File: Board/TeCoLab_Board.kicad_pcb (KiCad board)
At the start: 2 copper layers, 95.1 x 93.8 mm, 61 parts, among them J1 Jack, J2 Supply_Terminal, J3 DC Cooler, Q1 BC337, Q2 TIP122, Q3 TIP122, U1 DS18B20, U2 PC817, U3 DS18B20, U4 DS18B20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

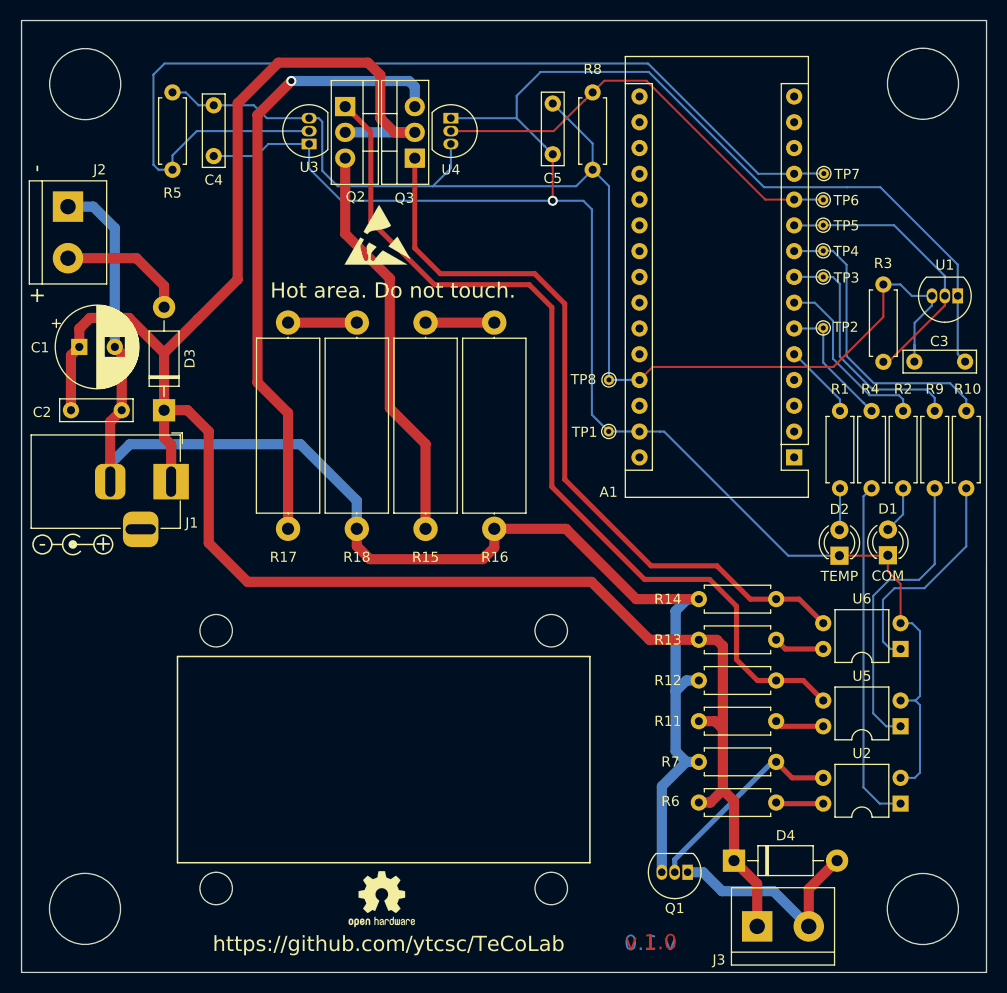
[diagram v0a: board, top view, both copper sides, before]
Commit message: Hardware: Update files to comply with KiCad version 8.0.
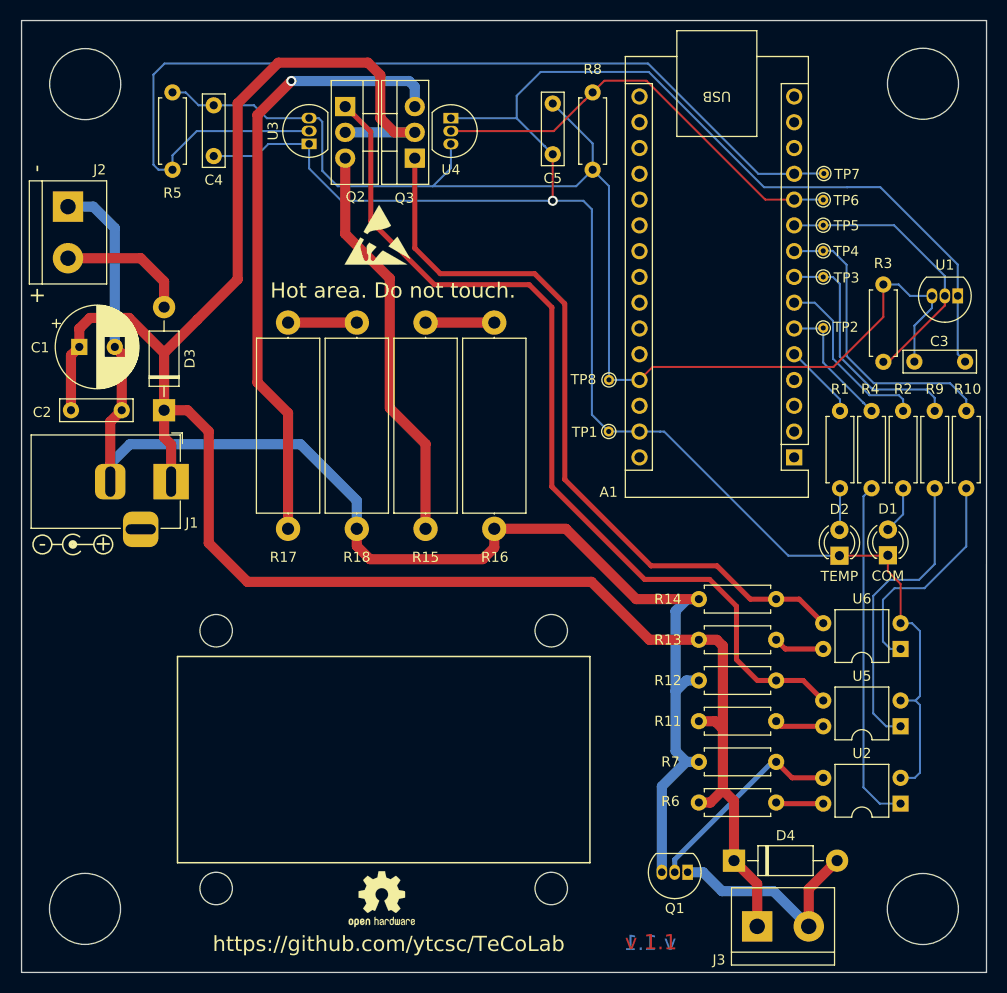
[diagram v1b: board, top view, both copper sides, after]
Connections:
- A1 pad 1: Net-(A1-Pad1) -> unconnected-(A1-D1/TX-Pad1)
- A1 pad 13: Net-(A1-Pad13) -> unconnected-(A1-D10-Pad13)
- A1 pad 14: Net-(A1-Pad14) -> unconnected-(A1-D11-Pad14)
- A1 pad 15: Net-(A1-Pad15) -> unconnected-(A1-D12-Pad15)
- A1 pad 16: Net-(A1-Pad16) -> unconnected-(A1-D13-Pad16)
- A1 pad 17: Net-(A1-Pad17) -> unconnected-(A1-3V3-Pad17)
- A1 pad 18: Net-(A1-Pad18) -> unconnected-(A1-AREF-Pad18)
- A1 pad 19: Net-(A1-Pad19) -> unconnected-(A1-A0-Pad19)
- A1 pad 2: Net-(A1-Pad2) -> unconnected-(A1-D0/RX-Pad2)
- A1 pad 20: Net-(A1-Pad20) -> unconnected-(A1-A1-Pad20)
- A1 pad 21: Net-(A1-Pad21) -> unconnected-(A1-A2-Pad21)
- A1 pad 22: Net-(A1-Pad22) -> unconnected-(A1-A3-Pad22)
- A1 pad 23: Net-(A1-Pad23) -> unconnected-(A1-A4-Pad23)
- A1 pad 24: Net-(A1-Pad24) -> unconnected-(A1-A5-Pad24)
- A1 pad 25: Net-(A1-Pad25) -> unconnected-(A1-A6-Pad25)
- A1 pad 26: Net-(A1-Pad26) -> unconnected-(A1-A7-Pad26)
- A1 pad 28: Net-(A1-Pad28) -> unconnected-(A1-~{RESET}-Pad28)
- A1 pad 3: Net-(A1-Pad3) -> unconnected-(A1-~{RESET}-Pad3)
- A1 pad 30: Net-(A1-Pad30) -> unconnected-(A1-VIN-Pad30)
- A1 pad 4: Net-(A1-Pad4) -> unconnected-(A1-GND-Pad4)
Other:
- net class Analog Signals removed
- net class Default removed
- net class Digital Signals removed
- net class Power removed
- board text added: "v 1.1"
- board text removed: "v 1.0"

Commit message: Update for KiCad 9.0 compatibility; remove gerbers from repository; Schematic: replaced 10K resistors by 4.7K resistors; PCB: replaced TO-92 package by its hand-soldering version.
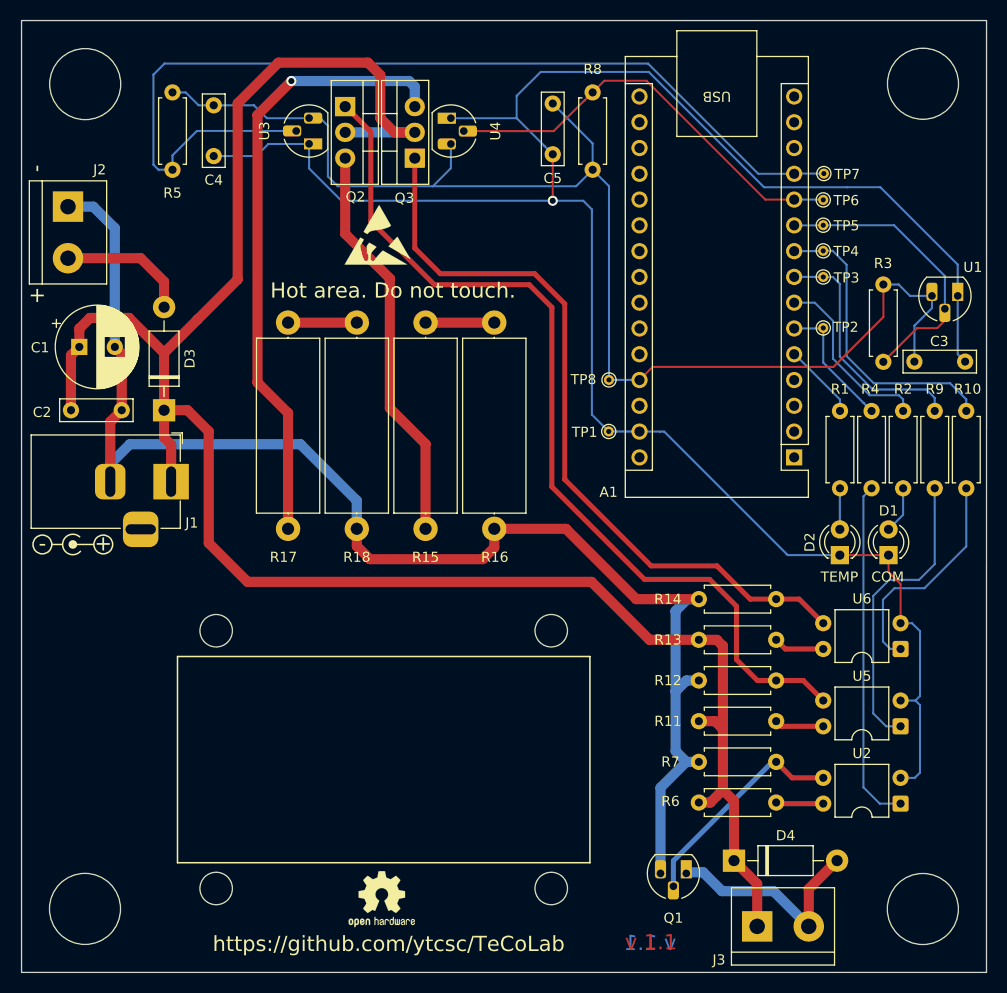
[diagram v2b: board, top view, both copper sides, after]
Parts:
- D1: value COM -> LED
- D2: value TEMP -> LED
- Q1, U1, U3, U4: footprint Package_TO_SOT_THT:TO-92_Inline -> Package_TO_SOT_THT:TO-92_HandSolder
- R3, R5, R7, R8: value 10K -> 4.7K
- moved Q1 0.17 mm to (171.3, 117.7)
- moved D1 0.07 mm to (191.2, 86.4)
- moved D2 0.06 mm to (186.4, 86.4)
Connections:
- net LED_GREEN renamed LED_green
- net LED_RED renamed LED_red
- net RoomTempSensor renamed Sensor_roomtemp
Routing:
- net +5V: track 128.4 -> 130.7 mm
- net Net-(Q1-B): track 20.5 -> 22.0 mm
- net Sensor_roomtemp: track 28.3 -> 29.7 mm
- net Sensor_2: track 43.7 -> 42.4 mm
- net Sensor_1: track 97.9 -> 96.7 mm
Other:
- board text added: "COM"
- board text added: "TEMP"
